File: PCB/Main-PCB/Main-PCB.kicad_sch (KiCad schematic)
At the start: 0 parts

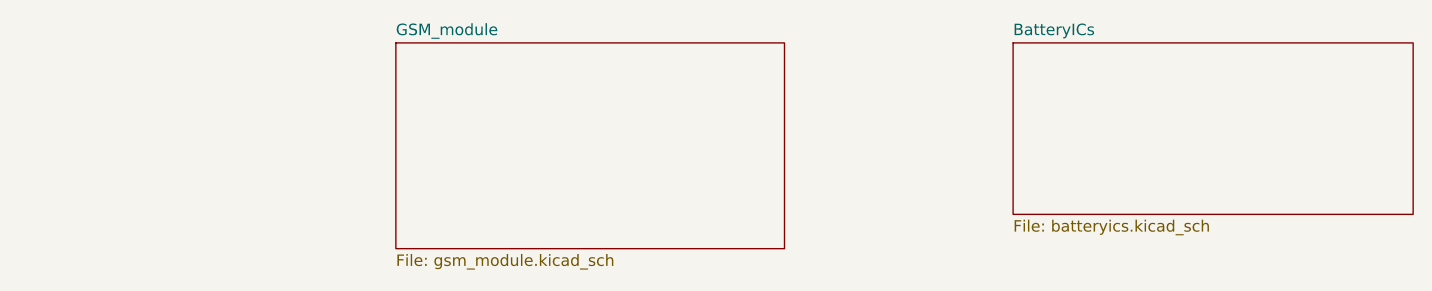
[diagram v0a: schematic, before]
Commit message: Finished schematic for SIM800C and power chips
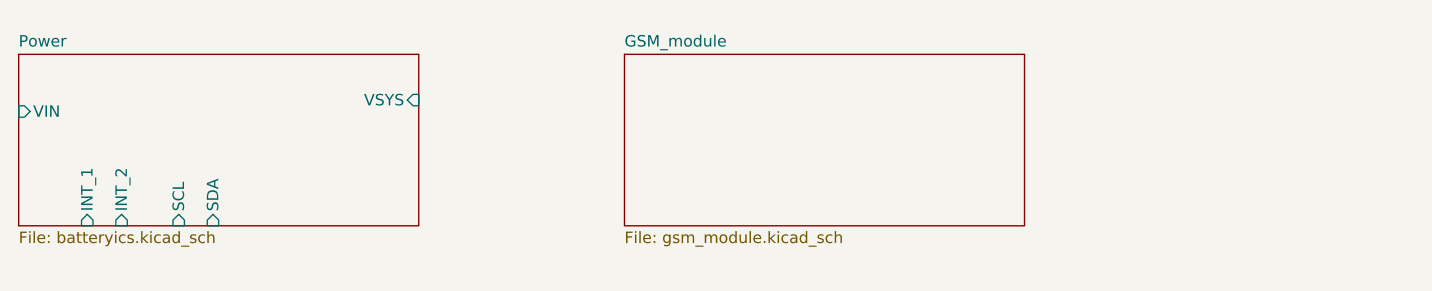
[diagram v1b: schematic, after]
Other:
- sheet BatteryICs renamed Power
- sheet Power ports: added INT_1, INT_2, SCL, SDA, VIN, VSYS; removed none
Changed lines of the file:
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@@
 	(paper "A4")
 	(sheet
-		(at 133.35 52.07)
+		(at 22.86 53.34)
 		(size 44.45 19.05)
 		(exclude_from_sim no)
@@
 			(color 0 0 0 0.0000)
 		)
-		(property "Sheetname" "BatteryICs"
-			(at 133.35 51.3584 0)
+		(property "Sheetname" "Power"
+			(at 22.86 52.6284 0)
 			(effects
 				(font
@@
 		)
 		(property "Sheetfile" "batteryics.kicad_sch"
-			(at 133.35 71.7046 0)
+			(at 22.86 72.9746 0)
 			(effects
 				(font
@@
 				)
 				(justify left top)
+			)
+		)
+		(pin "INT_1" input
+			(at 30.48 72.39 270)
+			(effects
+				(font
+					(size 1.27 1.27)
+				)
+				(justify left)
+			)
+		)
+		(pin "INT_2" input
+			(at 34.29 72.39 270)
+			(effects
+				(font
+					(size 1.27 1.27)
+				)
+				(justify left)
+			)
+		)
+		(pin "SCL" input
+			(at 40.64 72.39 270)
+			(effects
+				(font
+					(size 1.27 1.27)
+				)
+				(justify left)
+			)
+		)
+		(pin "SDA" input
+			(at 44.45 72.39 270)
+			(effects
+				(font
+					(size 1.27 1.27)
+				)
+				(justify left)
+			)
+		)
+		(pin "VIN" input
+			(at 22.86 59.69 180)
+			(effects
+				(font
+					(size 1.27 1.27)
+				)
+				(justify left)
+			)
+		)
+		(pin "VSYS" input
+			(at 67.31 58.42 0)
+			(effects
+				(font
+					(size 1.27 1.27)
+				)
+				(justify right)
 			)
 		)
@@
 	)
 	(sheet
-		(at 64.77 52.07)
-		(size 43.18 22.86)
+		(at 90.17 53.34)
+		(size 44.45 19.05)
 		(exclude_from_sim no)
 		(in_bom yes)
@@
 		)
 		(property "Sheetname" "GSM_module"
-			(at 64.77 51.3584 0)
+			(at 90.17 52.6284 0)
 			(effects
 				(font
@@
 		)
 		(property "Sheetfile" "gsm_module.kicad_sch"
-			(at 64.77 75.5146 0)
+			(at 90.17 72.9746 0)
 			(effects
 				(font

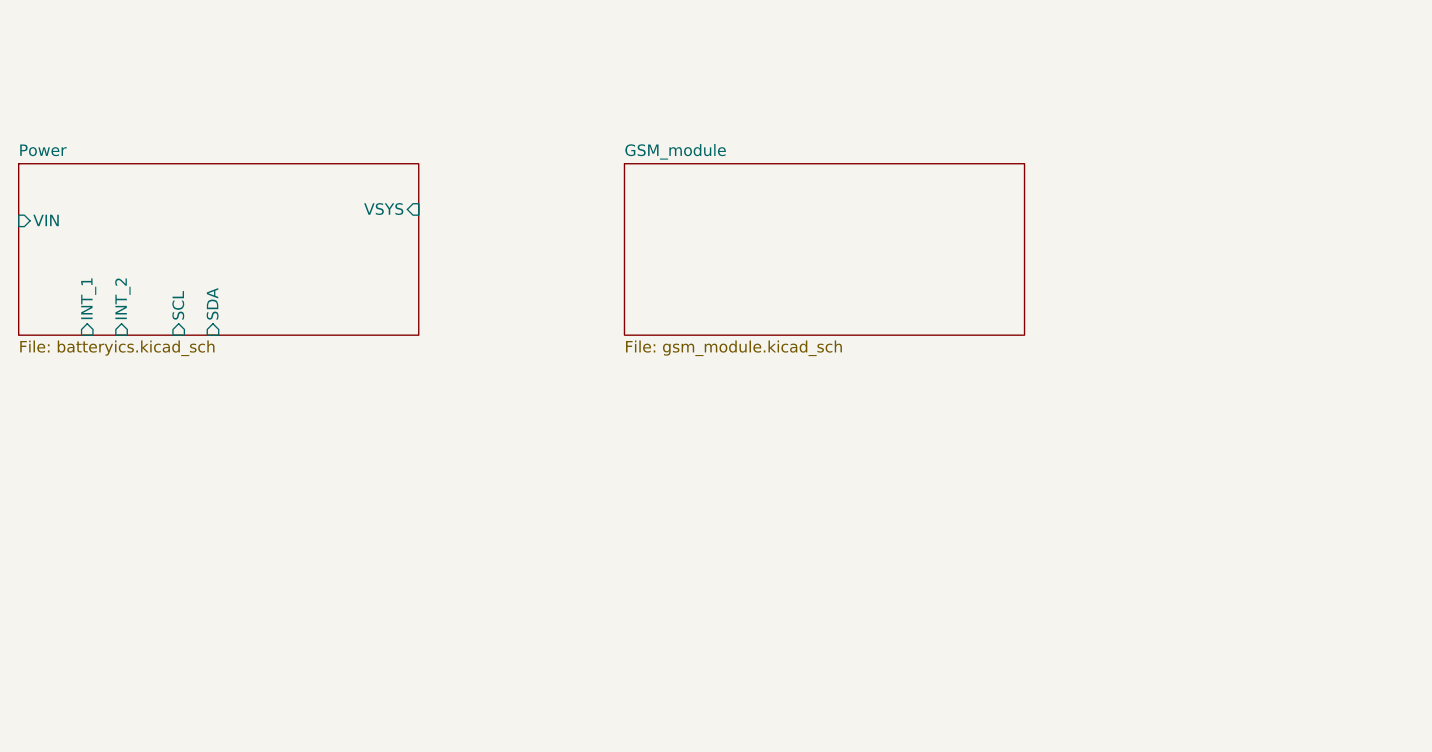
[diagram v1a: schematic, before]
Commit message: Added MCU scheme
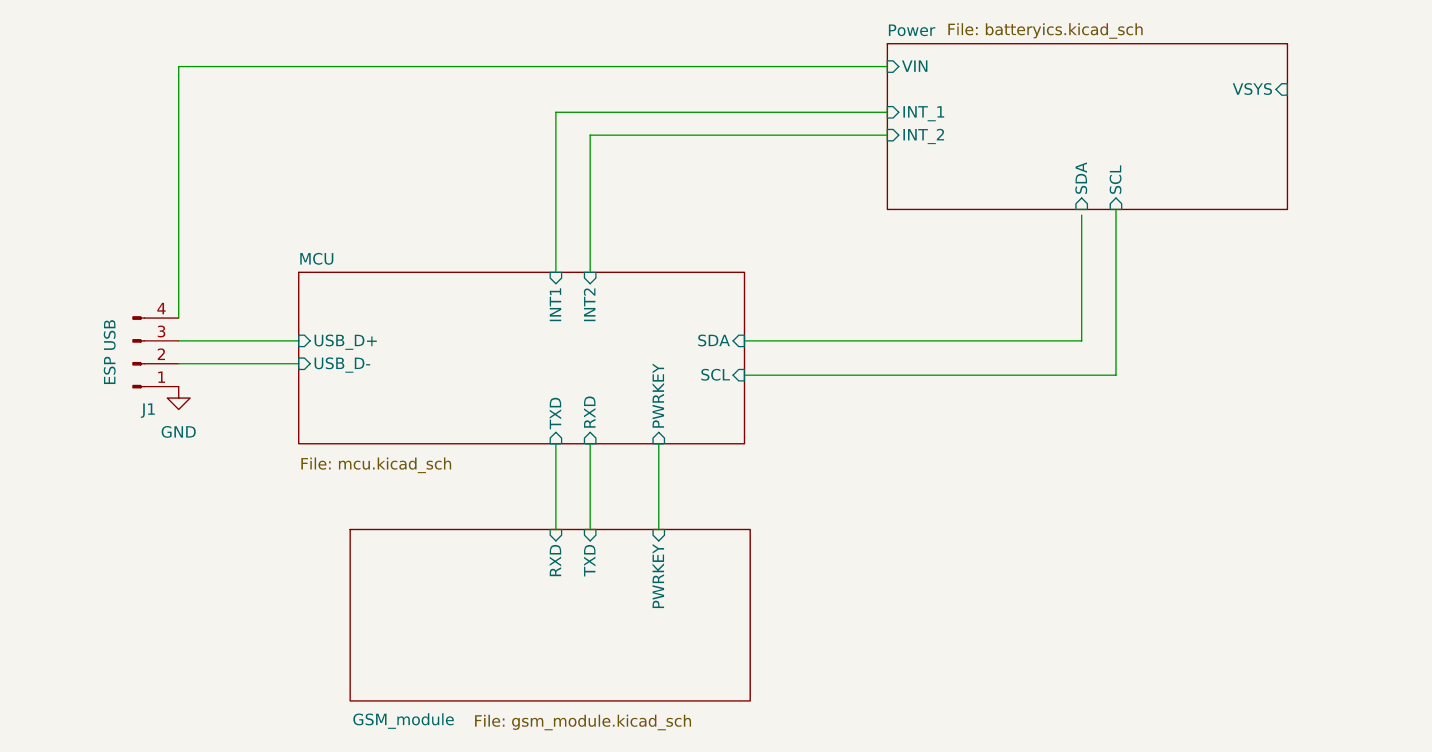
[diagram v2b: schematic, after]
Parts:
- added J1: ESP USB, symbol Connector:Conn_01x04_Pin
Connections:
- net Power/VIN: now also J1.4 (Pin_4)
- new net GND: J1.1 (Pin_1)
- new net MCU/USB_D+: J1.3 (Pin_3)
- new net MCU/USB_D-: J1.2 (Pin_2)
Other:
- added sheet MCU (mcu.kicad_sch)
- sheet GSM_module ports: added PWRKEY, RXD, TXD; removed none
